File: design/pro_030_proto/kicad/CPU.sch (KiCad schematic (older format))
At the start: 24 parts, among them IC1 MC68030RC_PGA, X1 CXO_DIP8

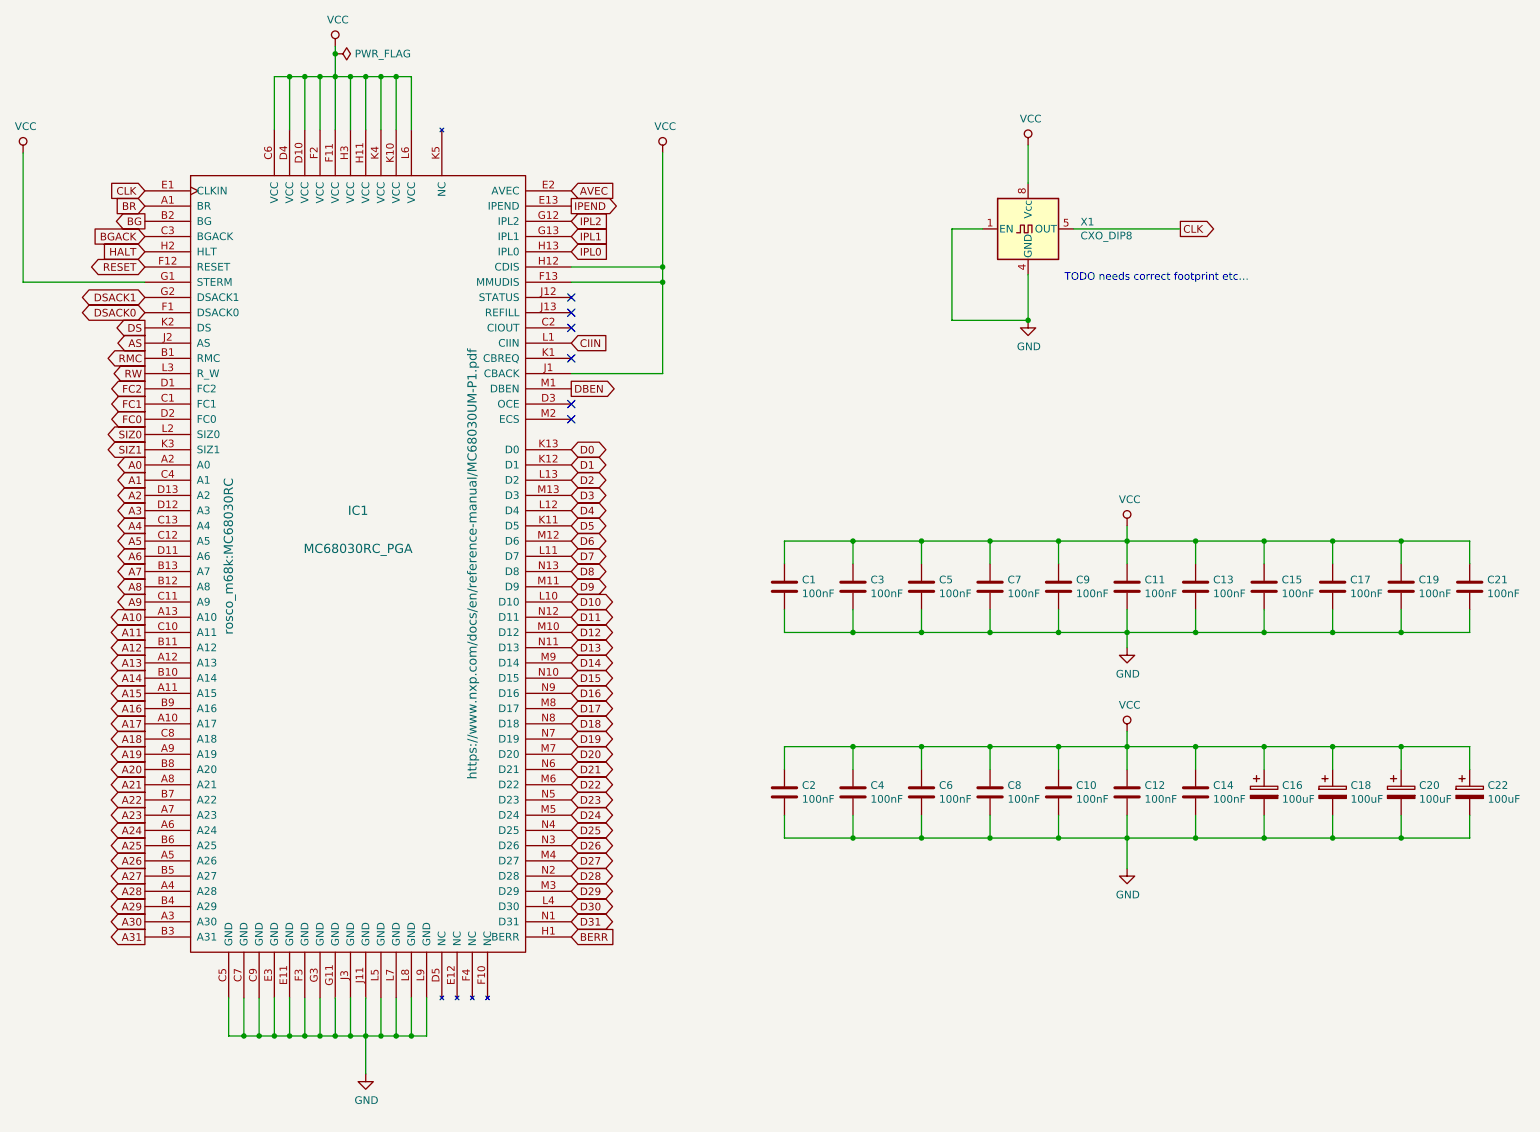
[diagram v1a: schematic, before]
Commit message: Largeish changeset:
* Added (first-cut) glue for DTACK generation
* Fix mem selects to use new DTACK generation
* Add missing footprints for Kicad
* Add POWER and TESTPOINTS schematics
* Update footprints across the board to allow error-free PCB import
* Pull all components (so far) into PCB
* Fix MC68030RC footprint (missing pads)
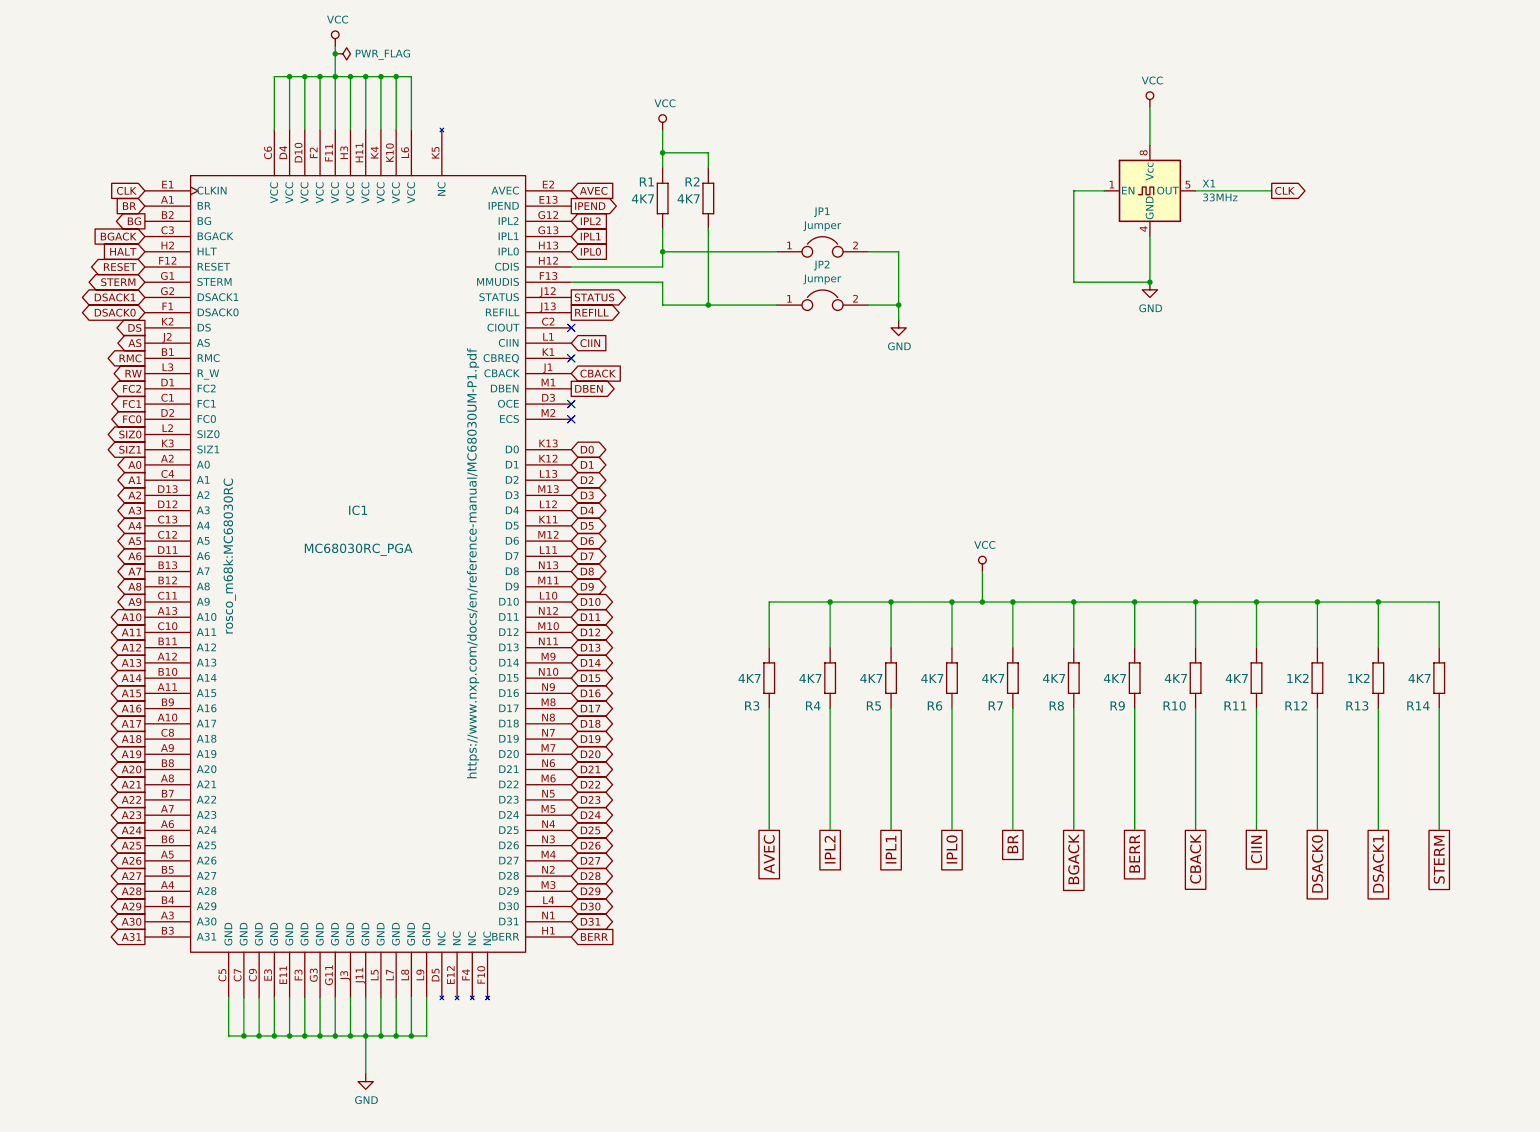
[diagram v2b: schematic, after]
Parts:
- removed C1, C10, C11, C12, C13, C14, C15, C17, C19, C2, C21, C3, C4, C5, C6, C7, C8, C9: 100nF, Capacitor_THT:C_Rect_L4.0mm_W2.5mm_P2.50mm, symbol Device:C
- removed C16, C18, C20, C22: 100uF, Capacitor_THT:CP_Radial_D5.0mm_P2.50mm, symbol Device:CP
- added JP1, JP2: Jumper, rosco_m68k:pin-1X02, symbol Device:Jumper
- added R1, R10, R11, R14, R2, R3, R4, R5, R6, R7, R8, R9: 4K7, rosco_m68k:R-0207_10, symbol rosco_m68k-eagle-import:R-EU_0207_10
- added R12, R13: 1K2, rosco_m68k:R-0207_10, symbol rosco_m68k-eagle-import:R-EU_0207_10
- X1: value CXO_DIP8 -> 33MHz
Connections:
- net AVEC: now also R3.1
- net BERR: now also R9.1
- net BGACK: now also R8.1
- net BR: now also R7.1
- net CIIN: now also R11.1
- net DSACK0: now also R12.1
- net DSACK1: now also R13.1
- net GND: now also JP1.2, JP2.2
- net IPL0: now also R6.1
- net IPL1: now also R5.1
- net IPL2: now also R4.1
- net VCC: now also R1.2, R10.2, R11.2, R12.2, R13.2, R14.2, R2.2, R3.2, R4.2, R5.2, R6.2, R7.2, R8.2, R9.2; no longer IC1.F13 (MMUDIS), IC1.G1 (STERM), IC1.H12 (CDIS), IC1.J1 (CBACK)
- net STATUS: now reaches IC1.J12 (STATUS)
- net REFILL: now reaches IC1.J13 (REFILL)
- new net: IC1.F13 (MMUDIS), JP2.1, R2.1
- new net: IC1.H12 (CDIS), JP1.1, R1.1
- new net CBACK: IC1.J1 (CBACK), R10.1
- new net STERM: IC1.G1 (STERM), R14.1
- no-connect marks 6 -> 4
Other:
- note removed: "TODO needs correct footprint etc…"
- moved on the sheet: X1

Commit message: Big(ish) push on placement
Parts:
- JP1: renamed from JP2; footprint rosco_m68k:pin-1X02 -> Connector_PinHeader_2.54mm:PinHeader_1x02_P2.54mm_Vertical
- JP2: renamed from JP1; footprint rosco_m68k:pin-1X02 -> Connector_PinHeader_2.54mm:PinHeader_1x02_P2.54mm_Vertical
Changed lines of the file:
@@
 $EndComp
 $Comp
-L Device:Jumper JP1
+L Device:Jumper JP2
 U 1 1 61161044
 P 6250 2050
-F 0 "JP1" H 6250 2314 50  0000 C CNN
+F 0 "JP2" H 6250 2314 50  0000 C CNN
 F 1 "Jumper" H 6250 2223 50  0000 C CNN
-F 2 "rosco_m68k:pin-1X02" H 6250 2050 50  0001 C CNN
+F 2 "Connector_PinHeader_2.54mm:PinHeader_1x02_P2.54mm_Vertical" H 6250 2050 50  0001 C CNN
 F 3 "~" H 6250 2050 50  0001 C CNN
 	1    6250 2050
@@
 $EndComp
 $Comp
-L Device:Jumper JP2
+L Device:Jumper JP1
 U 1 1 61161F89
 P 6250 2400
-F 0 "JP2" H 6250 2664 50  0000 C CNN
+F 0 "JP1" H 6250 2664 50  0000 C CNN
 F 1 "Jumper" H 6250 2573 50  0000 C CNN
-F 2 "rosco_m68k:pin-1X02" H 6250 2400 50  0001 C CNN
+F 2 "Connector_PinHeader_2.54mm:PinHeader_1x02_P2.54mm_Vertical" H 6250 2400 50  0001 C CNN
 F 3 "~" H 6250 2400 50  0001 C CNN
 	1    6250 2400

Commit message: Further layout
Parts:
- renumbered JP2 to JP1, JP1 to JP2
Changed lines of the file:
@@
 $EndComp
 $Comp
-L Device:Jumper JP2
+L Device:Jumper JP1
 U 1 1 61161044
 P 6250 2050
-F 0 "JP2" H 6250 2314 50  0000 C CNN
+F 0 "JP1" H 6250 2314 50  0000 C CNN
 F 1 "Jumper" H 6250 2223 50  0000 C CNN
 F 2 "Connector_PinHeader_2.54mm:PinHeader_1x02_P2.54mm_Vertical" H 6250 2050 50  0001 C CNN
@@
 $EndComp
 $Comp
-L Device:Jumper JP1
+L Device:Jumper JP2
 U 1 1 61161F89
 P 6250 2400
-F 0 "JP1" H 6250 2664 50  0000 C CNN
+F 0 "JP2" H 6250 2664 50  0000 C CNN
 F 1 "Jumper" H 6250 2573 50  0000 C CNN
 F 2 "Connector_PinHeader_2.54mm:PinHeader_1x02_P2.54mm_Vertical" H 6250 2400 50  0001 C CNN

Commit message: Finally fix ERC...
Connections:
- net CIOUT: now reaches IC1.C2 (CIOUT)
- net OCE: now reaches IC1.D3 (OCE)
- net MMUDIS: now reaches IC1.F13 (MMUDIS), JP2.1, R2.1
- net CDIS: now reaches IC1.H12 (CDIS), JP1.1, R1.1
- net CBREQ: now reaches IC1.K1 (CBREQ)
- net ECS: now reaches IC1.M2 (ECS)
- no-connect marks 4 -> 0
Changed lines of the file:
@@
 $EndDescr
-$Comp
-L power:GND #PWR02
-U 1 1 60A95AF5
-P 3250 7450
-F 0 "#PWR02" H 3250 7200 50  0001 C CNN
-F 1 "GND" H 3255 7277 50  0000 C CNN
-F 2 "" H 3250 7450 50  0001 C CNN
-F 3 "" H 3250 7450 50  0001 C CNN
-	1    3250 7450
-	1    0    0    -1
-$EndComp
 $Comp
 L power:VCC #PWR01
@@
 Wire Wire Line
 	2950 900  3050 900
-Wire Wire Line
-	3050 700  3050 750
 Wire Wire Line
 	2350 6950 2350 7200
@@
 $EndComp
 Wire Wire Line
-	4600 2150 5200 2150
-NoConn ~ 4600 2750
-NoConn ~ 4600 2550
-NoConn ~ 4600 3050
-NoConn ~ 4600 3150
+	4600 2150 5050 2150
 Text GLabel 4600 1750 2    50   Output ~ 0
 IPEND
-$Comp
-L power:PWR_FLAG #FLG01
-U 1 1 60C2B135
-P 3050 750
-F 0 "#FLG01" H 3050 825 50  0001 C CNN
-F 1 "PWR_FLAG" V 3050 878 50  0000 L CNN
-F 2 "" H 3050 750 50  0001 C CNN
-F 3 "~" H 3050 750 50  0001 C CNN
-	1    3050 750
-	0    1    1    0
-$EndComp
-Connection ~ 3050 750
-Wire Wire Line
-	3050 750  3050 900
 $Comp
 L Oscillator:CXO_DIP8 X1
@@
 CIIN
 Wire Wire Line
-	4600 2250 5200 2250
+	4600 2250 5050 2250
 $Comp
 L rosco_m68k-eagle-import:R-EU_0207_10 R?
@@
 Text GLabel 4600 2350 2    50   Output ~ 0
 STATUS
+Wire Wire Line
+	5050 2150 5050 2050
+Connection ~ 5050 2150
+Wire Wire Line
+	5050 2150 5200 2150
+Text GLabel 5050 2050 1    50   Output ~ 0
+CDIS
+Wire Wire Line
+	5050 2250 5050 2350
+Connection ~ 5050 2250
+Wire Wire Line
+	5050 2250 5200 2250
+Text GLabel 5050 2350 3    50   Output ~ 0
+MMUDIS
+Text GLabel 4600 3050 2    50   Input ~ 0
+OCE
+Text GLabel 4600 3150 2    50   Input ~ 0
+ECS
+Text GLabel 4600 2550 2    50   Output ~ 0
+CIOUT
+Text GLabel 4600 2750 2    50   Output ~ 0
+CBREQ
+Wire Wire Line
+	3050 700  3050 900
+Text GLabel 3250 7450 3    50   UnSpc ~ 0
+GND
 $EndSCHEMATC

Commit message: Fix some silly mistakes
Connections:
- net GND: no longer X1.1 (EN)
- net VCC: now also X1.1 (EN)
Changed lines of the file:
@@
 	8100 1650 7900 1650
 Wire Wire Line
-	7900 1650 7900 2250
-Wire Wire Line
-	7900 2250 8400 2250
-Wire Wire Line
 	8400 1950 8400 2250
-Connection ~ 8400 2250
-Wire Wire Line
-	8400 1100 8400 1350
+Wire Wire Line
+	8400 1100 8400 1250
 Text GLabel 4600 2650 2    50   Input ~ 0
 CIIN
@@
 Text GLabel 3250 7450 3    50   UnSpc ~ 0
 GND
+Wire Wire Line
+	7900 1650 7900 1250
+Wire Wire Line
+	7900 1250 8400 1250
+Connection ~ 8400 1250
+Wire Wire Line
+	8400 1250 8400 1350
 $EndSCHEMATC
